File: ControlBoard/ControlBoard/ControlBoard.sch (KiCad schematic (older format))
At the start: 6 parts

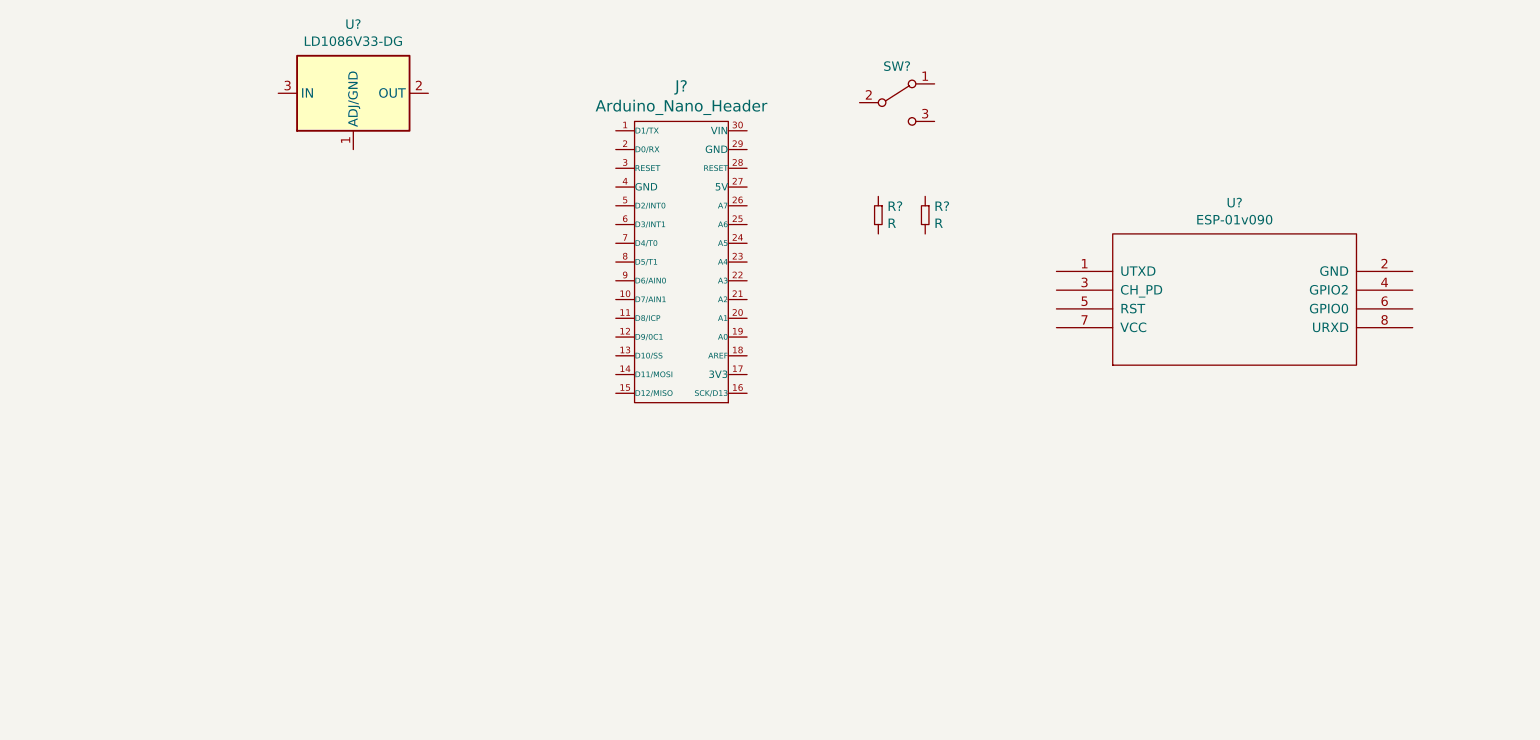
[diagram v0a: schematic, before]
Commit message: Implemento esquema, la misma se alimenta con una fuente externa de 3v3 para el esp, no considero regulador ya que tengo una fuente con ese voltaje
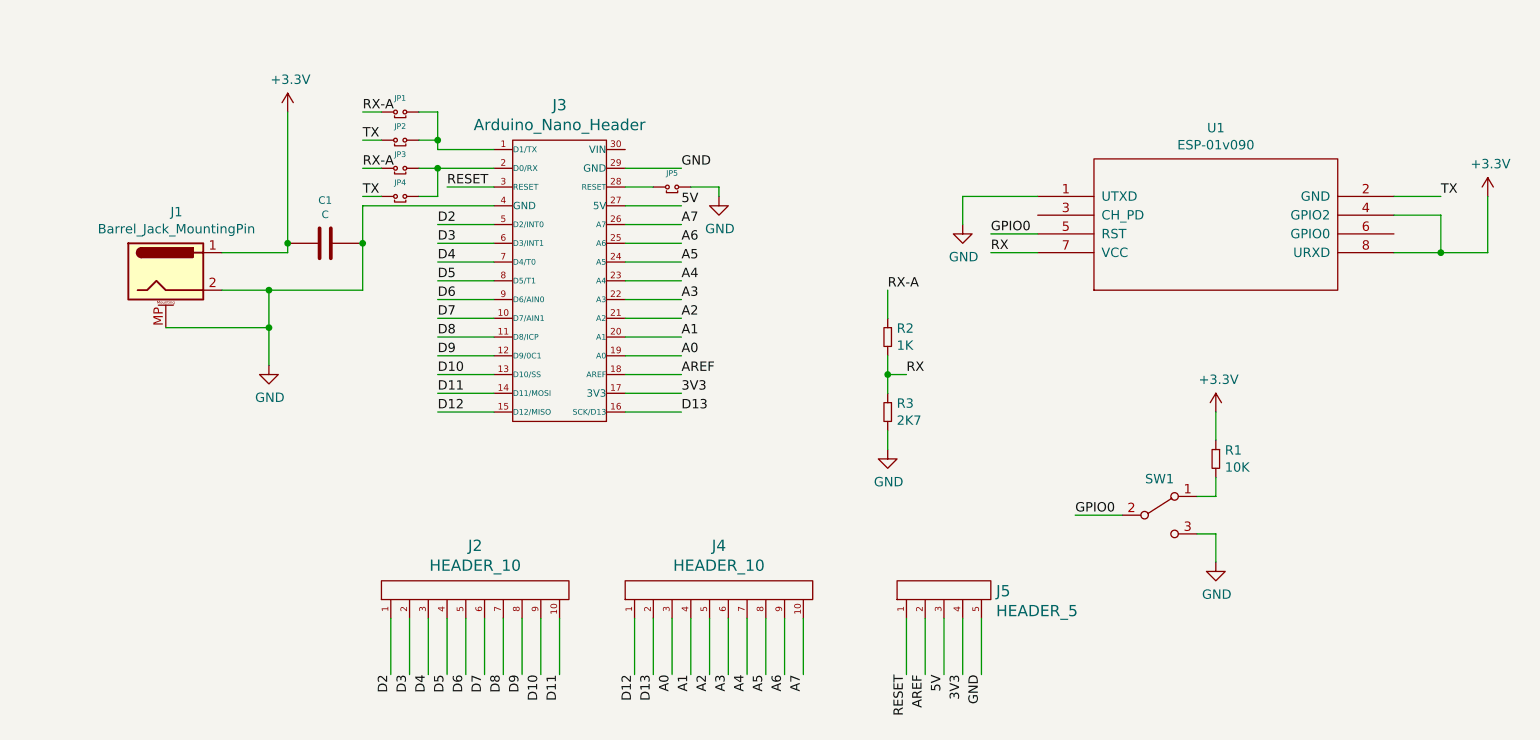
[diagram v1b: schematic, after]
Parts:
- removed U?: LD1086V33-DG, Package_TO_SOT_THT:TO-220-3_Vertical, symbol Regulator_Linear:LD1086V33-DG
- added C1: C, symbol EESTN5:C
- added J1: Barrel_Jack_MountingPin, symbol Connector:Barrel_Jack_MountingPin
- added J2, J4: HEADER_10, symbol EESTN5:HEADER_10
- added J5: HEADER_5, symbol EESTN5:HEADER_5
- added JP1, JP2, JP3, JP4, JP5: Jumper, symbol EESTN5:Jumper
- added R1: 10K, symbol EESTN5:R
- R2: renamed from R?; value R -> 1K
- R3: renamed from R?; value R -> 2K7
- gave numbers to parts that had none: 3
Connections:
- net at J3.1 (D1/TX): now also JP1.2 (B), JP2.2 (B)
- net D7: now reaches J3.10 (D7/AIN1)
- net D7: now also J2.6
- net D8: now reaches J3.11 (D8/ICP)
- net D8: now also J2.7
- net D9: now reaches J3.12 (D9/0C1)
- net D9: now also J2.8
- net D10: now reaches J3.13 (D10/SS)
- net D10: now also J2.9
- net D11: now reaches J3.14 (D11/MOSI)
- net D11: now also J2.10
- net D12: now reaches J3.15 (D12/MISO)
- net D12: now also J4.1
- net D13: now reaches J3.16 (SCK/D13)
- net D13: now also J4.2
- net 3V3: now reaches J3.17 (3V3)
- net 3V3: now also J5.4
- net AREF: now reaches J3.18 (AREF)
- net AREF: now also J5.2
- net A0: now reaches J3.19 (A0)
- net A0: now also J4.3
- net at J3.2 (D0/RX): now also JP3.2 (B), JP4.2 (B)
- net A1: now reaches J3.20 (A1)
- net A1: now also J4.4
- net A2: now reaches J3.21 (A2)
- net A2: now also J4.5
- net A3: now reaches J3.22 (A3)
- net A3: now also J4.6
- net A4: now reaches J3.23 (A4)
- net A4: now also J4.7
- net A5: now reaches J3.24 (A5)
- net A5: now also J4.8
- net A6: now reaches J3.25 (A6)
- net A6: now also J4.9
- net A7: now reaches J3.26 (A7)
- net A7: now also J4.10
- net 5V: now reaches J3.27 (5V)
- net 5V: now also J5.3
- net at J3.28 (RESET): now also JP5.1 (A)
- net GND: now reaches J3.29 (GND)
- net GND: now also J3.4 (GND), R3.2, SW1.3 (C), U1.1 (UTXD), C1.1, J1.2, J1.MP (MountPin), J5.5, JP5.2 (B)
- net RESET: now reaches J3.3 (RESET)
- net RESET: now also J5.1
- net D2: now reaches J3.5 (D2/INT0)
- net D2: now also J2.1
- net D3: now reaches J3.6 (D3/INT1)
- net D3: now also J2.2
- net D4: now reaches J3.7 (D4/T0)
- net D4: now also J2.3
- net D5: now reaches J3.8 (D5/T1)
- net D5: now also J2.4
- net D6: now reaches J3.9 (D6/AIN0)
- net D6: now also J2.5
- net TX: now reaches U1.2 (GND)
- net TX: now also JP2.1 (A), JP4.1 (A)
- net +3V3: now reaches U1.4 (GPIO2)
- net +3V3: now also U1.8 (URXD), C1.2, J1.1, R1.1
- net GPIO0: now reaches U1.5 (RST)
- net GPIO0: now also SW1.2 (B)
- net RX: now reaches U1.7 (VCC)
- net RX: now also R2.2, R3.1
- net at SW1.1 (A): now also R1.2
- net RX-A: now reaches R2.1
- net RX-A: now also JP1.1 (A), JP3.1 (A)
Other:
- moved on the sheet: J3, R2, R3, SW1, U1

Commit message: Agrego PCB + Comienzo de diseño
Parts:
- added D20: DIODE, EESTN5:DO-41, symbol EESTN5:DIODE
- C1: footprint (none) -> EESTN5:CAP_0.1
- J1: footprint (none) -> Connector_BarrelJack:BarrelJack_Horizontal
- J2, J4: footprint (none) -> EESTN5:Pin_Header_Straight_1x10
- J3: footprint (none) -> EESTN5:arduino_nano_header
- J5: footprint (none) -> EESTN5:Pin_Header_5
- JP1, JP2, JP3, JP4, JP5: footprint (none) -> EESTN5:Jumper
- R1, R2, R3: footprint (none) -> EESTN5:RES0.3
- SW1: footprint (none) -> EESTN5:SW_SPDT_TH_Vertical
- U1: footprint (none) -> ESP8266:ESP-01
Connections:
- net +3V3: now also D20.2 (K); no longer C1.2, J1.1
- new net: C1.2, D20.1 (A), J1.1
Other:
- moved on the sheet: C1, J1
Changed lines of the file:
@@
 F 0 "R3" H 6698 3646 50  0000 L CNN
 F 1 "2K7" H 6698 3555 50  0000 L CNN
-F 2 "" H 6650 3600 60  0001 C CNN
+F 2 "EESTN5:RES0.3" H 6650 3600 60  0001 C CNN
 F 3 "" H 6650 3600 60  0000 C CNN
 	1    6650 3600
@@
 F 0 "R2" H 6698 3246 50  0000 L CNN
 F 1 "1K" H 6698 3155 50  0000 L CNN
-F 2 "" H 6650 3200 60  0001 C CNN
+F 2 "EESTN5:RES0.3" H 6650 3200 60  0001 C CNN
 F 3 "" H 6650 3200 60  0000 C CNN
 	1    6650 3200
@@
 $EndComp
 $Comp
-L Connector:Barrel_Jack_MountingPin J1
-U 1 1 5FCEE4D5
-P 2800 2850
-F 0 "J1" H 2857 3167 50  0000 C CNN
-F 1 "Barrel_Jack_MountingPin" H 2857 3076 50  0000 C CNN
-F 2 "" H 2850 2810 50  0001 C CNN
-F 3 "~" H 2850 2810 50  0001 C CNN
-	1    2800 2850
-	1    0    0    -1
-$EndComp
-$Comp
 L EESTN5:C C1
 U 1 1 5FCF15FC
-P 3650 2700
-F 0 "C1" V 3421 2700 40  0000 C CNN
-F 1 "C" V 3497 2700 40  0000 C CNN
-F 2 "" H 3688 2550 30  0001 C CNN
-F 3 "" H 3650 2700 60  0000 C CNN
-	1    3650 2700
+P 3350 2650
+F 0 "C1" V 3121 2650 40  0000 C CNN
+F 1 "C" V 3197 2650 40  0000 C CNN
+F 2 "EESTN5:CAP_0.1" H 3388 2500 30  0001 C CNN
+F 3 "" H 3350 2650 60  0000 C CNN
+	1    3350 2650
 	0    1    1    0
 $EndComp
-Wire Wire Line
-	3100 2950 3350 2950
-Wire Wire Line
-	3850 2950 3850 2700
-Wire Wire Line
-	3850 2500 4550 2500
-Wire Wire Line
-	2800 3150 3350 3150
-Wire Wire Line
-	3350 3150 3350 2950
 Connection ~ 3350 2950
 Wire Wire Line
-	3350 2950 3850 2950
-Wire Wire Line
-	3450 2750 3450 2700
-Wire Wire Line
-	3100 2750 3450 2750
+	3350 2950 3550 2950
 $Comp
 L power:GND #PWR0102
@@
 	1    0    0    -1
 $EndComp
-Wire Wire Line
-	3350 3350 3350 3150
-Connection ~ 3350 3150
 $Comp
 L EESTN5:HEADER_10 J4
@@
 F 0 "J4" V 6037 4600 60  0000 C CNN
 F 1 "HEADER_10" V 5931 4600 60  0000 C CNN
-F 2 "" H 5750 5250 60  0001 C CNN
+F 2 "EESTN5:Pin_Header_Straight_1x10" H 5750 5250 60  0001 C CNN
 F 3 "" H 5750 5250 60  0000 C CNN
 	1    5750 4600
@@
 F 0 "J3" H 4900 3837 60  0000 C CNN
 F 1 "Arduino_Nano_Header" H 4900 3731 60  0000 C CNN
-F 2 "" H 4900 2900 60  0001 C CNN
+F 2 "EESTN5:arduino_nano_header" H 4900 2900 60  0001 C CNN
 F 3 "" H 4900 2900 60  0000 C CNN
 	1    4900 2900
@@
 F 0 "J2" V 4737 4600 60  0000 C CNN
 F 1 "HEADER_10" V 4631 4600 60  0000 C CNN
-F 2 "" H 4450 5250 60  0001 C CNN
+F 2 "EESTN5:Pin_Header_Straight_1x10" H 4450 5250 60  0001 C CNN
 F 3 "" H 4450 5250 60  0000 C CNN
 	1    4450 4600
@@
 F 0 "JP5" H 5500 2474 30  0000 C CNN
 F 1 "Jumper" H 5500 2450 30  0001 C CNN
-F 2 "" H 5500 2400 60  0001 C CNN
+F 2 "EESTN5:Jumper" H 5500 2400 60  0001 C CNN
 F 3 "" H 5500 2400 60  0000 C CNN
 	1    5500 2400
@@
 F 0 "R1" H 8448 3896 50  0000 L CNN
 F 1 "10K" H 8448 3805 50  0000 L CNN
-F 2 "" H 8400 3850 60  0001 C CNN
+F 2 "EESTN5:RES0.3" H 8400 3850 60  0001 C CNN
 F 3 "" H 8400 3850 60  0000 C CNN
 	1    8400 3850
@@
 F 0 "SW1" H 8100 4343 50  0000 C CNN
 F 1 "SW_SPDT" H 8100 3950 50  0001 C CNN
-F 2 "" H 8100 4150 50  0001 C CNN
+F 2 "EESTN5:SW_SPDT_TH_Vertical" H 8100 4150 50  0001 C CNN
 F 3 "" H 8100 4150 50  0000 C CNN
 	1    8100 4150
@@
 F 0 "U1" H 8400 3115 50  0000 C CNN
 F 1 "ESP-01v090" H 8400 3024 50  0000 C CNN
-F 2 "" H 8400 2600 50  0001 C CNN
+F 2 "ESP8266:ESP-01" H 8400 2600 50  0001 C CNN
 F 3 "http://l0l.org.uk/2014/12/esp8266-modules-hardware-guide-gotta-catch-em-all/" H 8400 2600 50  0001 C CNN
 	1    8400 2600
@@
 F 0 "JP2" H 4050 2224 30  0000 C CNN
 F 1 "Jumper" H 4050 2200 30  0001 C CNN
-F 2 "" H 4050 2150 60  0001 C CNN
+F 2 "EESTN5:Jumper" H 4050 2150 60  0001 C CNN
 F 3 "" H 4050 2150 60  0000 C CNN
 	1    4050 2150
@@
 F 0 "JP3" H 4050 2374 30  0000 C CNN
 F 1 "Jumper" H 4050 2350 30  0001 C CNN
-F 2 "" H 4050 2300 60  0001 C CNN
+F 2 "EESTN5:Jumper" H 4050 2300 60  0001 C CNN
 F 3 "" H 4050 2300 60  0000 C CNN
 	1    4050 2300
@@
 F 0 "JP1" H 4050 2074 30  0000 C CNN
 F 1 "Jumper" H 4050 2050 30  0001 C CNN
-F 2 "" H 4050 2000 60  0001 C CNN
+F 2 "EESTN5:Jumper" H 4050 2000 60  0001 C CNN
 F 3 "" H 4050 2000 60  0000 C CNN
 	1    4050 2000
@@
 F 0 "JP4" H 4050 2524 30  0000 C CNN
 F 1 "Jumper" H 4050 2500 30  0001 C CNN
-F 2 "" H 4050 2450 60  0001 C CNN
+F 2 "EESTN5:Jumper" H 4050 2450 60  0001 C CNN
 F 3 "" H 4050 2450 60  0000 C CNN
 	1    4050 2450
@@
 Wire Wire Line
 	6650 3100 6650 2950
-Connection ~ 3450 2700
-Wire Wire Line
-	3450 2700 3450 2000
-Connection ~ 3850 2700
-Wire Wire Line
-	3850 2700 3850 2500
+Wire Wire Line
+	3150 2650 3150 2100
 $Comp
 L power:+3.3V #PWR0108
 U 1 1 5FD7F79C
-P 3450 2000
-F 0 "#PWR0108" H 3450 1850 50  0001 C CNN
-F 1 "+3.3V" H 3465 2173 50  0000 C CNN
-F 2 "" H 3450 2000 50  0001 C CNN
-F 3 "" H 3450 2000 50  0001 C CNN
-	1    3450 2000
+P 3550 1950
+F 0 "#PWR0108" H 3550 1800 50  0001 C CNN
+F 1 "+3.3V" H 3565 2123 50  0000 C CNN
+F 2 "" H 3550 1950 50  0001 C CNN
+F 3 "" H 3550 1950 50  0001 C CNN
+	1    3550 1950
 	1    0    0    -1
 $EndComp
@@
 F 0 "J5" V 6995 4322 60  0000 R CNN
 F 1 "HEADER_5" V 6889 4322 60  0000 R CNN
-F 2 "" H 6950 5250 60  0001 C CNN
+F 2 "EESTN5:Pin_Header_5" H 6950 5250 60  0001 C CNN
 F 3 "" H 6950 5250 60  0000 C CNN
 	1    6950 4600
@@
 Wire Wire Line
 	7150 4700 7150 5000
+Connection ~ 3350 3150
+Wire Wire Line
+	3350 3350 3350 3150
+Wire Wire Line
+	3350 3150 3350 2950
+$Comp
+L Connector:Barrel_Jack_MountingPin J1
+U 1 1 5FCEE4D5
+P 2500 2850
+F 0 "J1" H 2557 3167 50  0000 C CNN
+F 1 "Barrel_Jack_MountingPin" H 2557 3076 50  0000 C CNN
+F 2 "Connector_BarrelJack:BarrelJack_Horizontal" H 2550 2810 50  0001 C CNN
+F 3 "~" H 2550 2810 50  0001 C CNN
+	1    2500 2850
+	1    0    0    -1
+$EndComp
+$Comp
+L EESTN5:DIODE D20
+U 1 1 5FDC9919
+P 3350 2100
+F 0 "D20" H 3350 2292 40  0000 C CNN
+F 1 "DIODE" H 3350 2216 40  0000 C CNN
+F 2 "EESTN5:DO-41" H 3350 2100 60  0001 C CNN
+F 3 "" H 3350 2100 60  0000 C CNN
+	1    3350 2100
+	1    0    0    -1
+$EndComp
+Wire Wire Line
+	2500 3150 3350 3150
+Wire Wire Line
+	2800 2950 3350 2950
+Wire Wire Line
+	2800 2750 3150 2750
+Wire Wire Line
+	3150 2750 3150 2650
+Wire Wire Line
+	3550 2500 3550 2650
+Connection ~ 3150 2650
+Connection ~ 3550 2650
+Wire Wire Line
+	3550 2650 3550 2950
+Wire Wire Line
+	3550 2500 4550 2500
+Wire Wire Line
+	3550 2100 3550 1950
 $EndSCHEMATC

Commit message: Concluyo diseño de ControlBoard
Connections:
- net +3V3: now also U1.3 (CH_PD), U1.7 (VCC); no longer U1.4 (GPIO2), U1.8 (URXD)
- net GND: now also U1.2 (GND); no longer U1.1 (UTXD)
- net GPIO0: now also U1.6 (GPIO0); no longer U1.5 (RST)
- net RX: now also U1.8 (URXD); no longer U1.7 (VCC)
- net TX: now also U1.1 (UTXD); no longer U1.2 (GND)
- net 5V: no longer names the net of J3.27 (5V)
- net 5V: no longer J5.3
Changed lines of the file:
@@
 Wire Wire Line
 	8300 4050 8400 4050
-$Comp
-L ESP8266:ESP-01v090 U1
-U 1 1 5FA3079A
-P 8400 2600
-F 0 "U1" H 8400 3115 50  0000 C CNN
-F 1 "ESP-01v090" H 8400 3024 50  0000 C CNN
-F 2 "ESP8266:ESP-01" H 8400 2600 50  0001 C CNN
-F 3 "http://l0l.org.uk/2014/12/esp8266-modules-hardware-guide-gotta-catch-em-all/" H 8400 2600 50  0001 C CNN
-	1    8400 2600
-	1    0    0    -1
-$EndComp
-Text Label 7200 2650 0    50   ~ 0
+Text Label 9600 2150 0    50   ~ 0
 GPIO0
 Wire Wire Line
-	7200 2650 7450 2650
-Wire Wire Line
-	7050 2450 7050 2600
+	9350 2150 9600 2150
 $Comp
 L power:GND #PWR0103
 U 1 1 5FCF92F0
-P 7050 2600
-F 0 "#PWR0103" H 7050 2350 50  0001 C CNN
-F 1 "GND" H 7055 2427 50  0000 C CNN
-F 2 "" H 7050 2600 50  0001 C CNN
-F 3 "" H 7050 2600 50  0001 C CNN
-	1    7050 2600
-	1    0    0    -1
-$EndComp
-Wire Wire Line
-	7050 2450 7450 2450
+P 9950 2050
+F 0 "#PWR0103" H 9950 1800 50  0001 C CNN
+F 1 "GND" H 9955 1877 50  0000 C CNN
+F 2 "" H 9950 2050 50  0001 C CNN
+F 3 "" H 9950 2050 50  0001 C CNN
+	1    9950 2050
+	1    0    0    -1
+$EndComp
 $Comp
 L power:+3.3V #PWR0106
 U 1 1 5FD3ABA1
-P 9850 2450
-F 0 "#PWR0106" H 9850 2300 50  0001 C CNN
-F 1 "+3.3V" H 9865 2623 50  0000 C CNN
-F 2 "" H 9850 2450 50  0001 C CNN
-F 3 "" H 9850 2450 50  0001 C CNN
-	1    9850 2450
-	1    0    0    -1
-$EndComp
-Wire Wire Line
-	9350 2750 9600 2750
-Wire Wire Line
-	9850 2750 9850 2450
-Text Label 7200 2750 0    50   ~ 0
+P 6950 1800
+F 0 "#PWR0106" H 6950 1650 50  0001 C CNN
+F 1 "+3.3V" H 6965 1973 50  0000 C CNN
+F 2 "" H 6950 1800 50  0001 C CNN
+F 3 "" H 6950 1800 50  0001 C CNN
+	1    6950 1800
+	1    0    0    -1
+$EndComp
+Text Label 9600 2250 0    50   ~ 0
 RX
-Text Label 9600 2450 0    50   ~ 0
+Text Label 7100 1950 0    50   ~ 0
 TX
 Wire Wire Line
-	7200 2750 7450 2750
-Wire Wire Line
-	9350 2450 9600 2450
-Wire Wire Line
-	9350 2550 9600 2550
-Wire Wire Line
-	9600 2550 9600 2750
-Connection ~ 9600 2750
-Wire Wire Line
-	9600 2750 9850 2750
+	9350 2250 9600 2250
 $Comp
 L power:GND #PWR0107
@@
 Text Label 5550 3400 0    50   ~ 0
 AREF
-Text Label 5550 2500 0    50   ~ 0
-5V
 Text Label 5550 2300 0    50   ~ 0
 GND
@@
 	5250 2300 5550 2300
 Wire Wire Line
-	5250 2500 5550 2500
-Wire Wire Line
 	5250 3400 5550 3400
 Wire Wire Line
@@
 Text Label 6850 5000 3    50   ~ 0
 AREF
-Text Label 6950 5000 3    50   ~ 0
-5V
 Text Label 7050 5000 3    50   ~ 0
 3V3
@@
 Wire Wire Line
 	6850 4700 6850 5000
-Wire Wire Line
-	6950 4700 6950 5000
 Wire Wire Line
 	7050 4700 7050 5000
@@
 Wire Wire Line
 	3550 2100 3550 1950
+$Comp
+L ESP8266:ESP-01v090 U1
+U 1 1 5FDDD9EA
+P 8400 2100
+F 0 "U1" H 8400 2615 50  0000 C CNN
+F 1 "ESP-01v090" H 8400 2524 50  0000 C CNN
+F 2 "ESP8266:ESP-01" H 8400 2100 50  0001 C CNN
+F 3 "http://l0l.org.uk/2014/12/esp8266-modules-hardware-guide-gotta-catch-em-all/" H 8400 2100 50  0001 C CNN
+	1    8400 2100
+	1    0    0    -1
+$EndComp
+Wire Wire Line
+	7450 1950 7100 1950
+Wire Wire Line
+	9950 1950 9950 2050
+Wire Wire Line
+	9350 1950 9950 1950
+Wire Wire Line
+	6950 2050 6950 1800
+Wire Wire Line
+	6950 2050 7450 2050
+Wire Wire Line
+	6950 2250 6950 2050
+Wire Wire Line
+	6950 2250 7450 2250
+Connection ~ 6950 2050
 $EndSCHEMATC
